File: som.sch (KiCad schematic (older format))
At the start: 31 parts, among them M1 SC606T

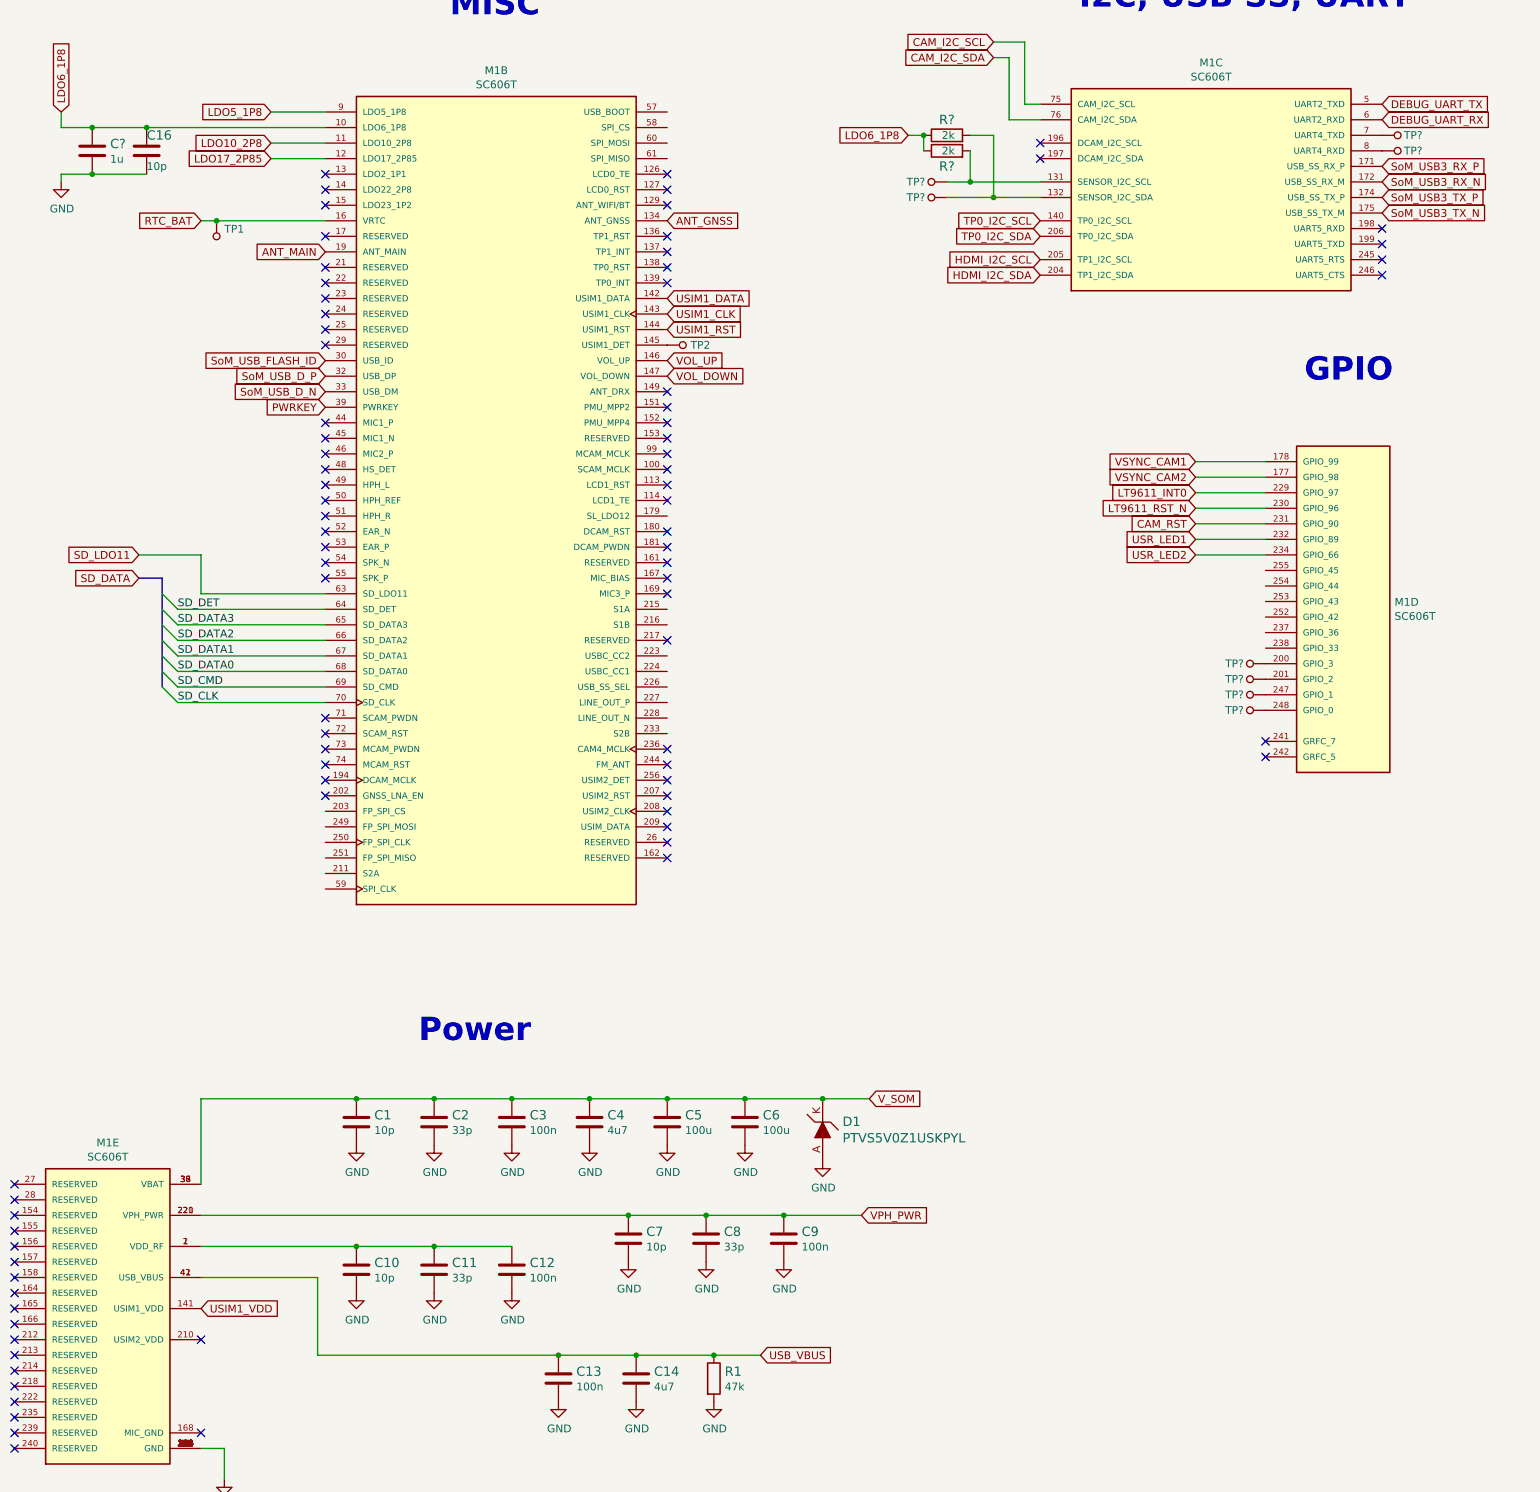
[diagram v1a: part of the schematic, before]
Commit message: Started placing main components on PCB. Change of RT battery model and USB flash connector
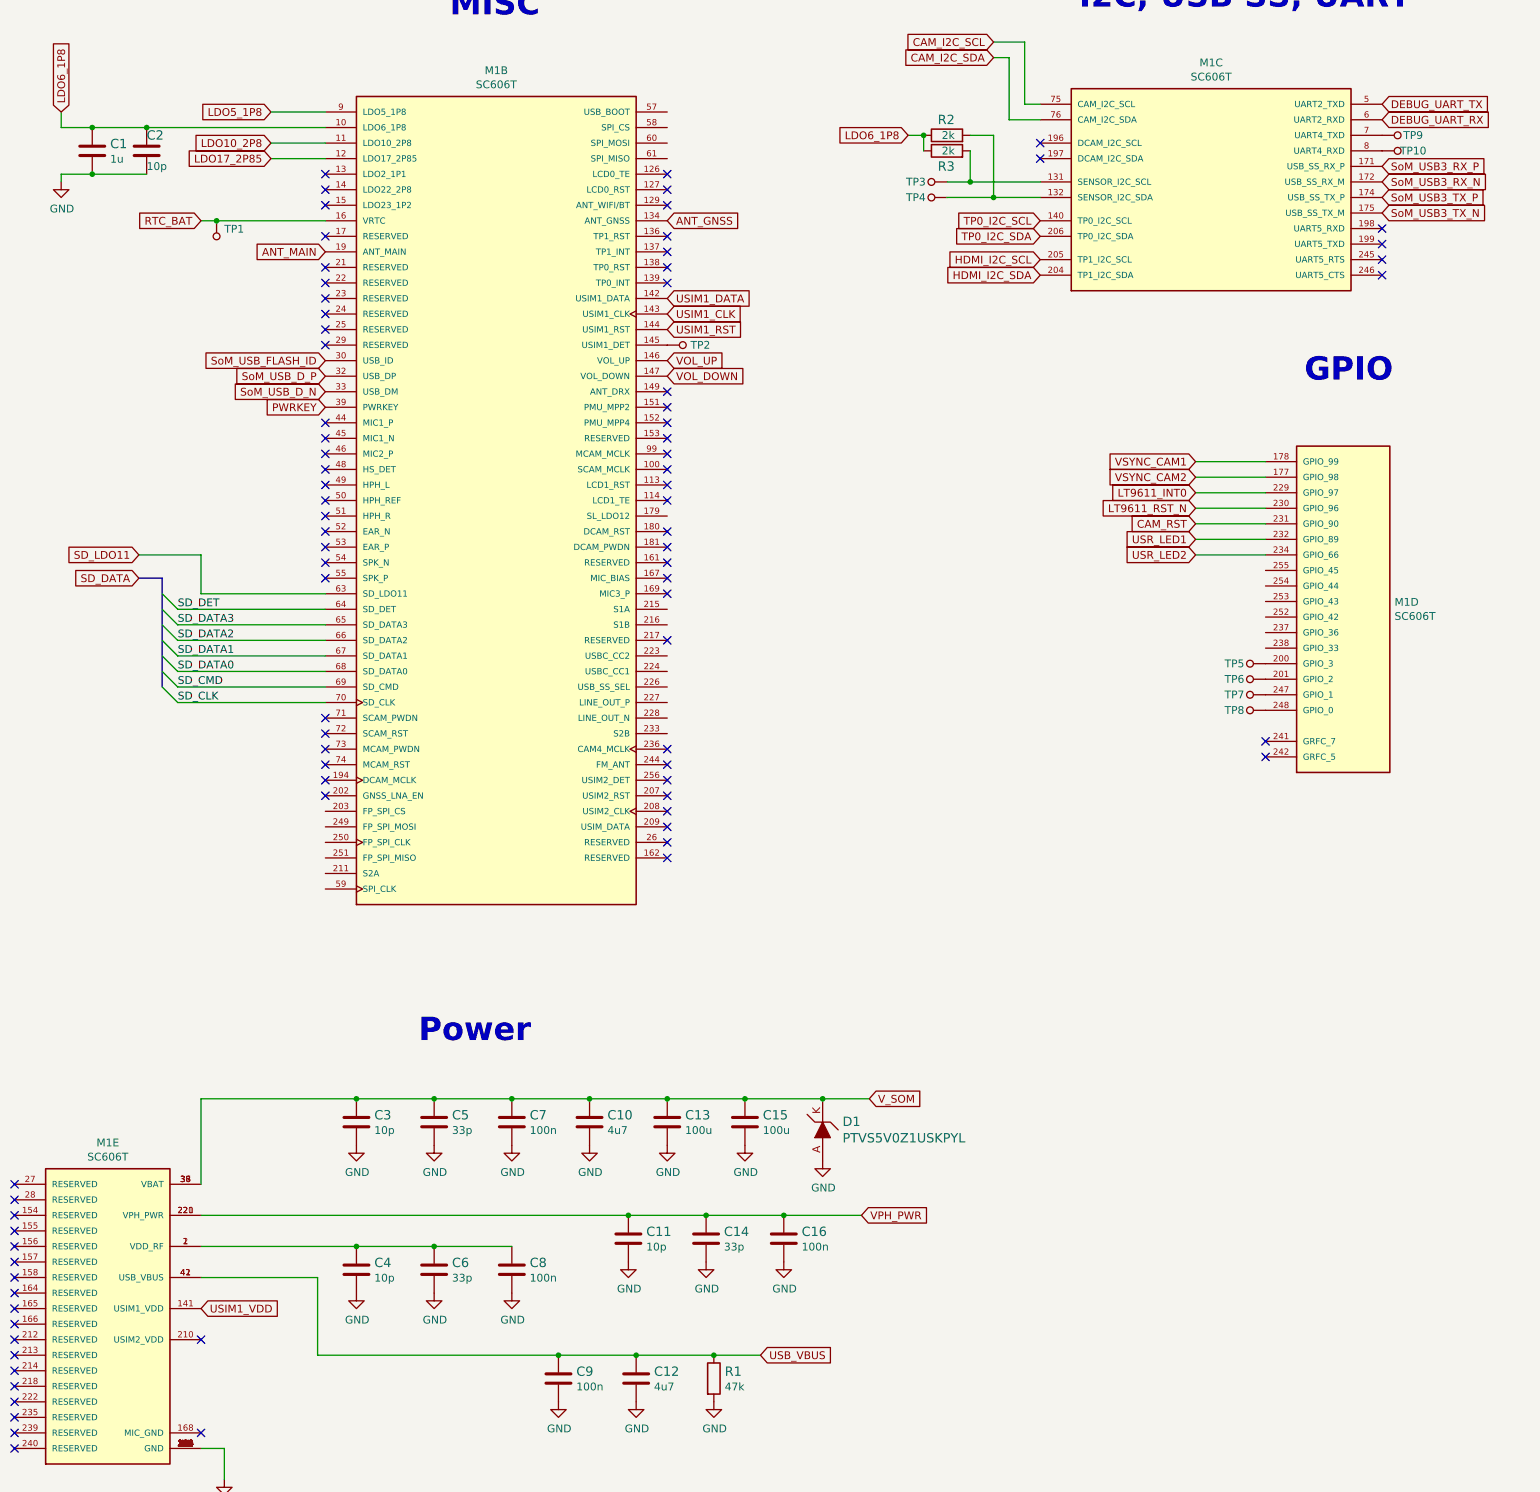
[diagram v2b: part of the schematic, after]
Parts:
- gave numbers to parts that had none: 11
- renumbered C4 to C10, C7 to C11, C14 to C12, C5 to C13, C8 to C14, C6 to C15, C9 to C16, C16 to C2, C1 to C3, C10 to C4, C2 to C5, C11 to C6, C3 to C7, C12 to C8, C13 to C9
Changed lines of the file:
@@
 V_SOM
 $Comp
-L sc606-baseboard:C_10p_0402 C1
+L sc606-baseboard:C_10p_0402 C3
 U 1 1 61FCFAC1
 P 3000 8150
-F 0 "C1" H 3115 8195 60  0000 L CNN
+F 0 "C3" H 3115 8195 60  0000 L CNN
 F 1 "C_10p_0402" H 3000 8000 60  0001 C CNN
 F 2 "sc606-baseboard-footprints:0402-cap" H 3200 8350 60  0001 L CNN
@@
 $EndComp
 $Comp
-L sc606-baseboard:C_33p_0402 C2
+L sc606-baseboard:C_33p_0402 C5
 U 1 1 61FD10EC
 P 3500 8150
-F 0 "C2" H 3615 8195 60  0000 L CNN
+F 0 "C5" H 3615 8195 60  0000 L CNN
 F 1 "C_33p_0402" H 3500 8000 60  0001 C CNN
 F 2 "sc606-baseboard-footprints:0402-cap" H 3700 8350 60  0001 L CNN
@@
 $EndComp
 $Comp
-L sc606-baseboard:C_100n_0402 C3
+L sc606-baseboard:C_100n_0402 C7
 U 1 1 61FD2DBE
 P 4000 8150
-F 0 "C3" H 4115 8195 60  0000 L CNN
+F 0 "C7" H 4115 8195 60  0000 L CNN
 F 1 "C_100n_0402" H 4000 8000 60  0001 C CNN
 F 2 "sc606-baseboard-footprints:0402-cap" H 4200 8350 60  0001 L CNN
@@
 $EndComp
 $Comp
-L sc606-baseboard:C_4u7_0402 C4
+L sc606-baseboard:C_4u7_0402 C10
 U 1 1 61FD43E8
 P 4500 8150
-F 0 "C4" H 4615 8195 60  0000 L CNN
+F 0 "C10" H 4615 8195 60  0000 L CNN
 F 1 "C_4u7_0402" H 4500 8000 60  0001 C CNN
 F 2 "sc606-baseboard-footprints:0402-cap" H 4700 8350 60  0001 L CNN
@@
 $EndComp
 $Comp
-L sc606-baseboard:C_100u_1206 C5
+L sc606-baseboard:C_100u_1206 C13
 U 1 1 61FD9566
 P 5000 8150
-F 0 "C5" H 5115 8195 60  0000 L CNN
+F 0 "C13" H 5115 8195 60  0000 L CNN
 F 1 "C_100u_1206" H 5000 8000 60  0001 C CNN
 F 2 "sc606-baseboard-footprints:1206-cap" H 5200 8350 60  0001 L CNN
@@
 $EndComp
 $Comp
-L sc606-baseboard:C_100u_1206 C6
+L sc606-baseboard:C_100u_1206 C15
 U 1 1 61FF8F26
 P 5500 8150
-F 0 "C6" H 5615 8195 60  0000 L CNN
+F 0 "C15" H 5615 8195 60  0000 L CNN
 F 1 "C_100u_1206" H 5500 8000 60  0001 C CNN
 F 2 "sc606-baseboard-footprints:1206-cap" H 5700 8350 60  0001 L CNN
@@
 $EndComp
 $Comp
-L sc606-baseboard:C_10p_0402 C7
+L sc606-baseboard:C_10p_0402 C11
 U 1 1 620A8D78
 P 4750 8900
-F 0 "C7" H 4865 8945 60  0000 L CNN
+F 0 "C11" H 4865 8945 60  0000 L CNN
 F 1 "C_10p_0402" H 4750 8750 60  0001 C CNN
 F 2 "sc606-baseboard-footprints:0402-cap" H 4950 9100 60  0001 L CNN
@@
 $EndComp
 $Comp
-L sc606-baseboard:C_33p_0402 C8
+L sc606-baseboard:C_33p_0402 C14
 U 1 1 620A8D81
 P 5250 8900
-F 0 "C8" H 5365 8945 60  0000 L CNN
+F 0 "C14" H 5365 8945 60  0000 L CNN
 F 1 "C_33p_0402" H 5250 8750 60  0001 C CNN
 F 2 "sc606-baseboard-footprints:0402-cap" H 5450 9100 60  0001 L CNN
@@
 $EndComp
 $Comp
-L sc606-baseboard:C_100n_0402 C9
+L sc606-baseboard:C_100n_0402 C16
 U 1 1 620A8D8A
 P 5750 8900
-F 0 "C9" H 5865 8945 60  0000 L CNN
+F 0 "C16" H 5865 8945 60  0000 L CNN
 F 1 "C_100n_0402" H 5750 8750 60  0001 C CNN
 F 2 "sc606-baseboard-footprints:0402-cap" H 5950 9100 60  0001 L CNN
@@
 VPH_PWR
 $Comp
-L sc606-baseboard:C_10p_0402 C10
+L sc606-baseboard:C_10p_0402 C4
 U 1 1 620E32C0
 P 3000 9100
-F 0 "C10" H 3115 9145 60  0000 L CNN
+F 0 "C4" H 3115 9145 60  0000 L CNN
 F 1 "C_10p_0402" H 3000 8950 60  0001 C CNN
 F 2 "sc606-baseboard-footprints:0402-cap" H 3200 9300 60  0001 L CNN
@@
 $EndComp
 $Comp
-L sc606-baseboard:C_33p_0402 C11
+L sc606-baseboard:C_33p_0402 C6
 U 1 1 620E32C9
 P 3500 9100
-F 0 "C11" H 3615 9145 60  0000 L CNN
+F 0 "C6" H 3615 9145 60  0000 L CNN
 F 1 "C_33p_0402" H 3500 8950 60  0001 C CNN
 F 2 "sc606-baseboard-footprints:0402-cap" H 3700 9300 60  0001 L CNN
@@
 $EndComp
 $Comp
-L sc606-baseboard:C_100n_0402 C12
+L sc606-baseboard:C_100n_0402 C8
 U 1 1 620E32D2
 P 4000 9100
-F 0 "C12" H 4115 9145 60  0000 L CNN
+F 0 "C8" H 4115 9145 60  0000 L CNN
 F 1 "C_100n_0402" H 4000 8950 60  0001 C CNN
 F 2 "sc606-baseboard-footprints:0402-cap" H 4200 9300 60  0001 L CNN
@@
 USIM1_VDD
 $Comp
-L sc606-baseboard:C_100n_0402 C13
+L sc606-baseboard:C_100n_0402 C9
 U 1 1 6210B3FC
 P 4300 9800
-F 0 "C13" H 4415 9845 60  0000 L CNN
+F 0 "C9" H 4415 9845 60  0000 L CNN
 F 1 "C_100n_0402" H 4300 9650 60  0001 C CNN
 F 2 "sc606-baseboard-footprints:0402-cap" H 4500 10000 60  0001 L CNN
@@
 $EndComp
 $Comp
-L sc606-baseboard:C_4u7_0402 C14
+L sc606-baseboard:C_4u7_0402 C12
 U 1 1 6210B405
 P 4800 9800
-F 0 "C14" H 4915 9845 60  0000 L CNN
+F 0 "C12" H 4915 9845 60  0000 L CNN
 F 1 "C_4u7_0402" H 4800 9650 60  0001 C CNN
 F 2 "sc606-baseboard-footprints:0402-cap" H 5000 10000 60  0001 L CNN
@@
 LDO6_1P8
 $Comp
-L sc606-baseboard:C_10p_0402 C16
+L sc606-baseboard:C_10p_0402 C2
 U 1 1 61FBFA62
 P 1650 1900
-F 0 "C16" H 1650 2000 60  0000 L CNN
+F 0 "C2" H 1650 2000 60  0000 L CNN
 F 1 "C_10p_0402" H 1650 1750 60  0001 C CNN
 F 2 "sc606-baseboard-footprints:0402-cap" H 1850 2100 60  0001 L CNN
@@
 	8850 4200 8400 4200
 $Comp
-L sc606-baseboard:C_1u_0402 C?
+L sc606-baseboard:C_1u_0402 C1
 U 1 1 61E5A12B
 P 1300 1900
-F 0 "C?" H 1415 1945 60  0000 L CNN
+F 0 "C1" H 1415 1945 60  0000 L CNN
 F 1 "C_1u_0402" H 1300 1750 60  0001 C CNN
 F 2 "sc606-baseboard-footprints:0402-cap" H 1500 2100 60  0001 L CNN
@@
 AR Path="/61D49F95/61EA9379" Ref="R?"  Part="1"
 AR Path="/61D49FBF/61EA9379" Ref="R?"  Part="1"
-AR Path="/61D43102/61EA9379" Ref="R?"  Part="1"
-F 0 "R?" H 6850 1900 60  0000 R CNN
+AR Path="/61D43102/61EA9379" Ref="R2"  Part="1"
+F 0 "R2" H 6850 1900 60  0000 R CNN
 F 1 "R_2k_0402" H 6800 1650 60  0001 C CNN
 F 2 "sc606-baseboard-footprints:0402-res" H 7000 2000 60  0001 L CNN
@@
 AR Path="/61D49F95/61EA9382" Ref="R?"  Part="1"
 AR Path="/61D49FBF/61EA9382" Ref="R?"  Part="1"
-AR Path="/61D43102/61EA9382" Ref="R?"  Part="1"
-F 0 "R?" H 6850 1800 60  0000 R CNN
+AR Path="/61D43102/61EA9382" Ref="R3"  Part="1"
+F 0 "R3" H 6850 1800 60  0000 R CNN
 F 1 "R_2k_0402" H 6800 1750 60  0001 C CNN
 F 2 "sc606-baseboard-footprints:0402-res" H 7000 2100 60  0001 L CNN
@@
 SoM_USB_D_N
 $Comp
-L sc606-baseboard:TP_SMD_0_75MM TP?
+L sc606-baseboard:TP_SMD_0_75MM TP8
 U 1 1 629CED8C
 P 8750 5500
-F 0 "TP?" V 8750 5400 50  0000 C CNN
+F 0 "TP8" V 8750 5400 50  0000 C CNN
 F 1 "TP_SMD_0_75MM" H 8750 5400 50  0001 C CNN
 F 2 "sc606-baseboard-footprints:Testpoint_smd_0_75mm" H 8950 5700 60  0001 L CNN
@@
 $EndComp
 $Comp
-L sc606-baseboard:TP_SMD_0_75MM TP?
+L sc606-baseboard:TP_SMD_0_75MM TP5
 U 1 1 629CF8B7
 P 8750 5200
-F 0 "TP?" V 8750 5100 50  0000 C CNN
+F 0 "TP5" V 8750 5100 50  0000 C CNN
 F 1 "TP_SMD_0_75MM" H 8750 5100 50  0001 C CNN
 F 2 "sc606-baseboard-footprints:Testpoint_smd_0_75mm" H 8950 5400 60  0001 L CNN
@@
 $EndComp
 $Comp
-L sc606-baseboard:TP_SMD_0_75MM TP?
+L sc606-baseboard:TP_SMD_0_75MM TP6
 U 1 1 629D5152
 P 8750 5300
-F 0 "TP?" V 8750 5200 50  0000 C CNN
+F 0 "TP6" V 8750 5200 50  0000 C CNN
 F 1 "TP_SMD_0_75MM" H 8750 5200 50  0001 C CNN
 F 2 "sc606-baseboard-footprints:Testpoint_smd_0_75mm" H 8950 5500 60  0001 L CNN
@@
 $EndComp
 $Comp
-L sc606-baseboard:TP_SMD_0_75MM TP?
+L sc606-baseboard:TP_SMD_0_75MM TP7
 U 1 1 629DAAF2
 P 8750 5400
-F 0 "TP?" V 8750 5300 50  0000 C CNN
+F 0 "TP7" V 8750 5300 50  0000 C CNN
 F 1 "TP_SMD_0_75MM" H 8750 5300 50  0001 C CNN
 F 2 "sc606-baseboard-footprints:Testpoint_smd_0_75mm" H 8950 5600 60  0001 L CNN
@@
 $EndComp
 $Comp
-L sc606-baseboard:TP_SMD_0_75MM TP?
+L sc606-baseboard:TP_SMD_0_75MM TP4
 U 1 1 629E615E
 P 6700 2200
-F 0 "TP?" V 6700 2100 50  0000 C CNN
+F 0 "TP4" V 6700 2100 50  0000 C CNN
 F 1 "TP_SMD_0_75MM" H 6700 2100 50  0001 C CNN
 F 2 "sc606-baseboard-footprints:Testpoint_smd_0_75mm" H 6900 2400 60  0001 L CNN
@@
 $EndComp
 $Comp
-L sc606-baseboard:TP_SMD_0_75MM TP?
+L sc606-baseboard:TP_SMD_0_75MM TP3
 U 1 1 629F6108
 P 6700 2100
-F 0 "TP?" V 6700 2000 50  0000 C CNN
+F 0 "TP3" V 6700 2000 50  0000 C CNN
 F 1 "TP_SMD_0_75MM" H 6700 2000 50  0001 C CNN
 F 2 "sc606-baseboard-footprints:Testpoint_smd_0_75mm" H 6900 2300 60  0001 L CNN
@@
 $EndComp
 $Comp
-L sc606-baseboard:TP_SMD_0_75MM TP?
+L sc606-baseboard:TP_SMD_0_75MM TP9
 U 1 1 629FCB71
 P 9700 1800
-F 0 "TP?" V 9700 1700 50  0000 C CNN
+F 0 "TP9" V 9700 1700 50  0000 C CNN
 F 1 "TP_SMD_0_75MM" H 9700 1700 50  0001 C CNN
 F 2 "sc606-baseboard-footprints:Testpoint_smd_0_75mm" H 9900 2000 60  0001 L CNN
@@
 $EndComp
 $Comp
-L sc606-baseboard:TP_SMD_0_75MM TP?
+L sc606-baseboard:TP_SMD_0_75MM TP10
 U 1 1 629FCB77
 P 9700 1900
-F 0 "TP?" V 9700 1800 50  0000 C CNN
+F 0 "TP10" V 9700 1800 50  0000 C CNN
 F 1 "TP_SMD_0_75MM" H 9700 1800 50  0001 C CNN
 F 2 "sc606-baseboard-footprints:Testpoint_smd_0_75mm" H 9900 2100 60  0001 L CNN

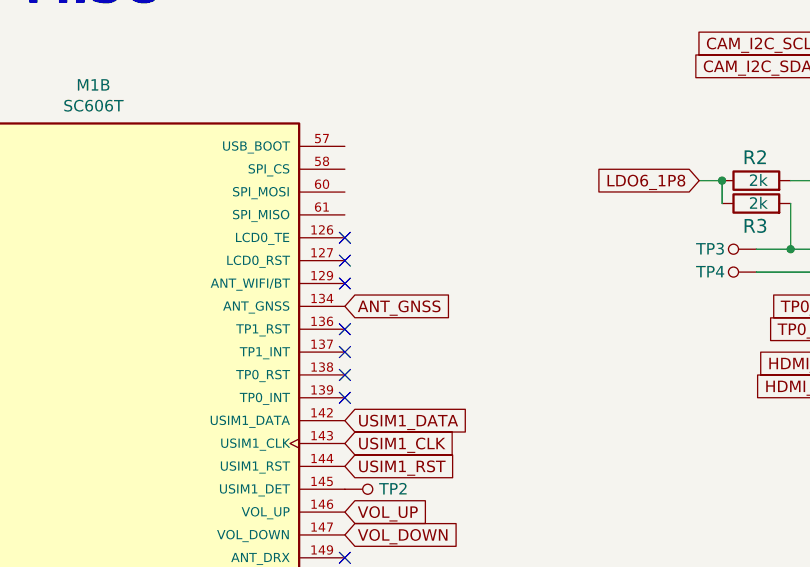
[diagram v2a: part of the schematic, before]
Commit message: Added USB A and C double stack connector
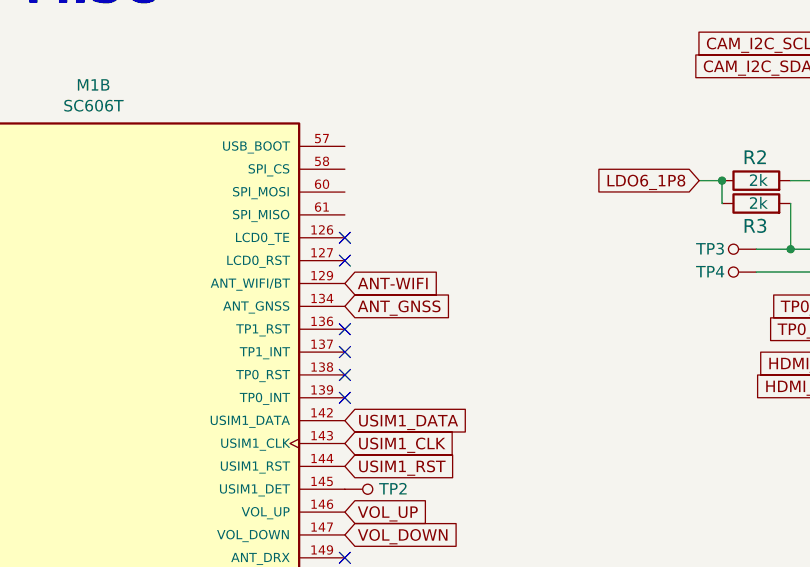
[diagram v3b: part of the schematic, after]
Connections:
- net ANT-WIFI: now reaches M1.129 (ANT_WIFI/BT)
- no-connect marks 94 -> 93
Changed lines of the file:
@@
 NoConn ~ 5000 2750
 NoConn ~ 5000 2650
-NoConn ~ 5000 2250
 NoConn ~ 5000 2450
 NoConn ~ 5000 2550
@@
 NoConn ~ 2800 2150
 NoConn ~ 2800 2250
+Text GLabel 5000 2250 2    50   Input ~ 0
+ANT-WIFI
 Wire Bus Line
 	1750 4650 1750 5350
